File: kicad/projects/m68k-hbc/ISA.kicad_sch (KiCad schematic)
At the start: 2 parts, among them J3 Bus_ISA_16bit, J4 Bus_ISA_16bit

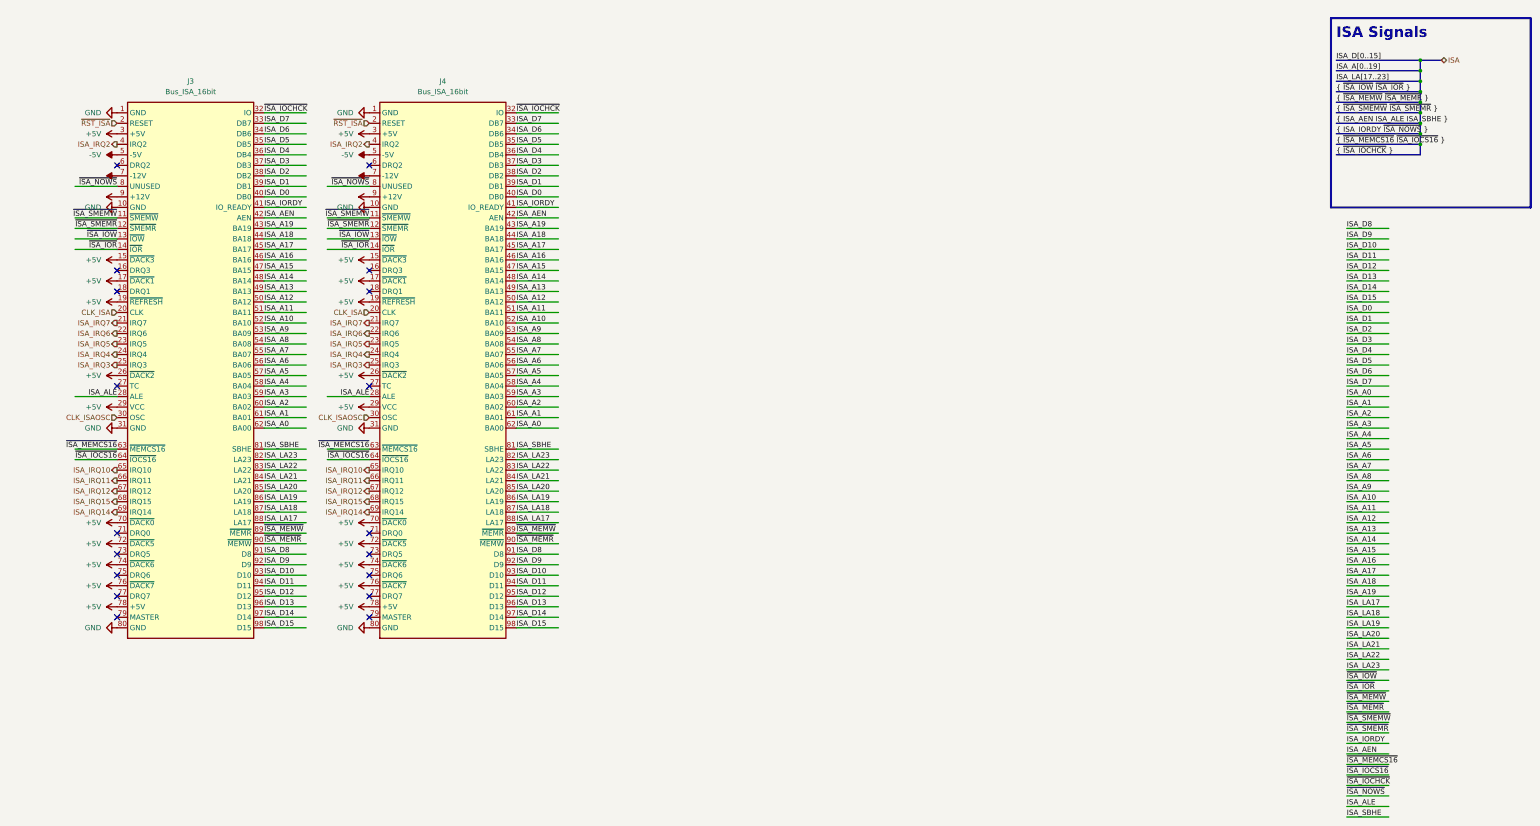
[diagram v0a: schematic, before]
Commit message: Large changes: EHBCSimpleEmu, kicad, fwcode, docs
This commit contains some large changes:
- Removed EHBCSimpleEmu (Moved to kms1212/llemu, kms1212/qemu)
- (likely) Removed fwcode; now it only boots and stops
- Modified documents
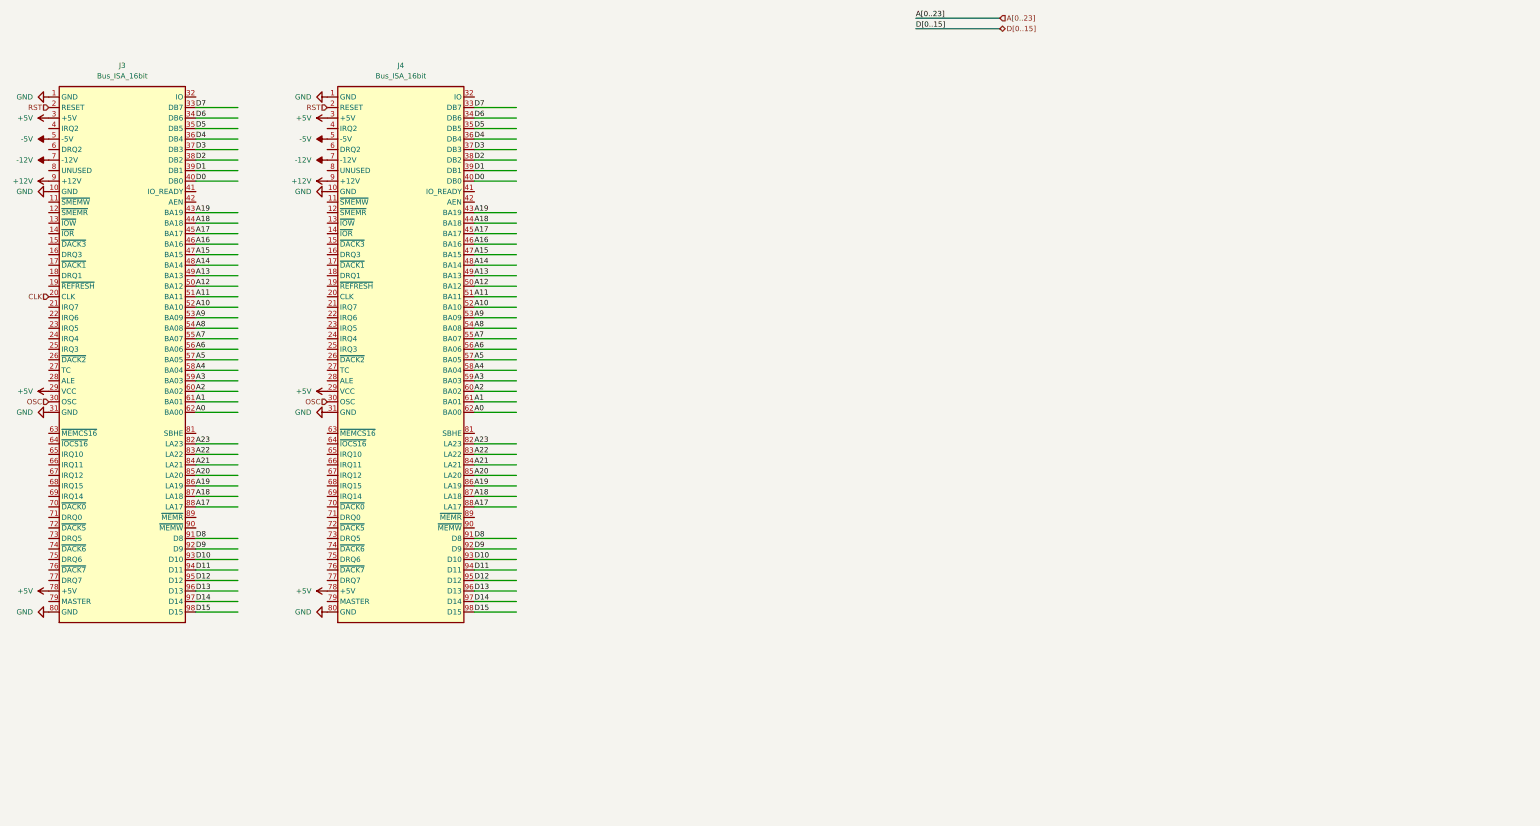
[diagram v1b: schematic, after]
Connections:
- net ISA_LA17 is gone; now on net A17: J3.88 (LA17), J4.88 (LA17)
- net ISA_LA18 is gone; now on net A18: J3.87 (LA18), J4.87 (LA18)
- net ISA_LA19 is gone; now on net A19: J3.86 (LA19), J4.86 (LA19)
- net +5V: no longer J3.15 (~{DACK3}), J3.17 (~{DACK1}), J3.19 (~{REFRESH}), J3.26 (~{DACK2}), J3.70 (~{DACK0}), J3.72 (~{DACK5}), J3.74 (~{DACK6}), J3.76 (~{DACK7}), J4.15 (~{DACK3}), J4.17 (~{DACK1}), J4.19 (~{REFRESH}), J4.26 (~{DACK2}), J4.70 (~{DACK0}), J4.72 (~{DACK5}), J4.74 (~{DACK6}), J4.76 (~{DACK7})
- net CLK_ISA: no longer names the net of J4.20 (CLK)
- net CLK_ISA: no longer J3.20 (CLK)
- net CLK_ISAOSC renamed OSC
- net ISA_A0 renamed A0
- net ISA_A1 renamed A1
- net ISA_A10 renamed A10
- net ISA_A11 renamed A11
- net ISA_A12 renamed A12
- net ISA_A13 renamed A13
- net ISA_A14 renamed A14
- net ISA_A15 renamed A15
- net ISA_A16 renamed A16
- net ISA_A17 renamed A17
- net ISA_A18 renamed A18
- net ISA_A19 renamed A19
- net ISA_A2 renamed A2
- net ISA_A3 renamed A3
- net ISA_A4 renamed A4
- net ISA_A5 renamed A5
- net ISA_A6 renamed A6
- net ISA_A7 renamed A7
- net ISA_A8 renamed A8
- net ISA_A9 renamed A9
- net ISA_AEN: no longer names the net of J3.42 (AEN)
- net ISA_AEN: no longer J4.42 (AEN)
- net ISA_ALE: no longer names the net of J3.28 (ALE)
- net ISA_ALE: no longer J4.28 (ALE)
- net ISA_D0 renamed D0
- net ISA_D1 renamed D1
- net ISA_D10 renamed D10
- net ISA_D11 renamed D11
- net ISA_D12 renamed D12
- net ISA_D13 renamed D13
- net ISA_D14 renamed D14
- net ISA_D15 renamed D15
- net ISA_D2 renamed D2
- net ISA_D3 renamed D3
- net ISA_D4 renamed D4
- net ISA_D5 renamed D5
- net ISA_D6 renamed D6
- net ISA_D7 renamed D7
- net ISA_D8 renamed D8
- net ISA_D9 renamed D9
- net ISA_IORDY: no longer names the net of J3.41 (IO_READY)
- net ISA_IORDY: no longer J4.41 (IO_READY)
- net ISA_IRQ10: no longer names the net of J3.65 (IRQ10)
- net ISA_IRQ10: no longer J4.65 (IRQ10)
- net ISA_IRQ11: no longer names the net of J3.66 (IRQ11)
- net ISA_IRQ11: no longer J4.66 (IRQ11)
- net ISA_IRQ12: no longer names the net of J3.67 (IRQ12)
- net ISA_IRQ12: no longer J4.67 (IRQ12)
- net ISA_IRQ14: no longer names the net of J3.69 (IRQ14)
- net ISA_IRQ14: no longer J4.69 (IRQ14)
- net ISA_IRQ15: no longer names the net of J3.68 (IRQ15)
- net ISA_IRQ15: no longer J4.68 (IRQ15)
- net ISA_IRQ2: no longer names the net of J3.4 (IRQ2)
- net ISA_IRQ2: no longer J4.4 (IRQ2)
- net ISA_IRQ3: no longer names the net of J3.25 (IRQ3)
- net ISA_IRQ3: no longer J4.25 (IRQ3)
- net ISA_IRQ4: no longer names the net of J3.24 (IRQ4)
- net ISA_IRQ4: no longer J4.24 (IRQ4)
- net ISA_IRQ5: no longer names the net of J3.23 (IRQ5)
- net ISA_IRQ5: no longer J4.23 (IRQ5)
- net ISA_IRQ6: no longer names the net of J3.22 (IRQ6)
- net ISA_IRQ6: no longer J4.22 (IRQ6)
- net ISA_IRQ7: no longer names the net of J3.21 (IRQ7)
- net ISA_IRQ7: no longer J4.21 (IRQ7)
- net ISA_LA20 renamed A20
- net ISA_LA21 renamed A21
- net ISA_LA22 renamed A22
- net ISA_LA23 renamed A23
- net ISA_SBHE: no longer names the net of J3.81 (SBHE)
- net ISA_SBHE: no longer J4.81 (SBHE)
- net ~{ISA_IOCHCK}: no longer names the net of J3.32 (IO)
- net ~{ISA_IOCHCK}: no longer J4.32 (IO)
- net ~{ISA_IOCS16}: no longer names the net of J3.64 (~{IOCS16})
- net ~{ISA_IOCS16}: no longer J4.64 (~{IOCS16})
- net ~{ISA_IOR}: no longer names the net of J3.14 (~{IOR})
- net ~{ISA_IOR}: no longer J4.14 (~{IOR})
- net ~{ISA_IOW}: no longer names the net of J3.13 (~{IOW})
- net ~{ISA_IOW}: no longer J4.13 (~{IOW})
- net ~{ISA_MEMCS16}: no longer names the net of J3.63 (~{MEMCS16})
- net ~{ISA_MEMCS16}: no longer J4.63 (~{MEMCS16})
- net ~{ISA_MEMR}: no longer names the net of J3.90 (~{MEMW})
- net ~{ISA_MEMR}: no longer J4.90 (~{MEMW})
- net ~{ISA_MEMW}: no longer names the net of J3.89 (~{MEMR})
- net ~{ISA_MEMW}: no longer J4.89 (~{MEMR})
- net ~{ISA_NOWS}: no longer names the net of J3.8 (UNUSED)
- net ~{ISA_NOWS}: no longer J4.8 (UNUSED)
- net ~{ISA_SMEMR}: no longer names the net of J3.12 (~{SMEMR})
- net ~{ISA_SMEMR}: no longer J4.12 (~{SMEMR})
- net ~{ISA_SMEMW}: no longer names the net of J3.11 (~{SMEMW})
- net ~{ISA_SMEMW}: no longer J4.11 (~{SMEMW})
- net ~{RST_ISA} renamed RST
- new net CLK: J3.20 (CLK)
- no-connect marks 18 -> 0
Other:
- note removed: "ISA Signals"
